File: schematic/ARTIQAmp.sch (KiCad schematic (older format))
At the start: 9 parts, among them J1 Power conneciton, J2 HD68, J3 HD68

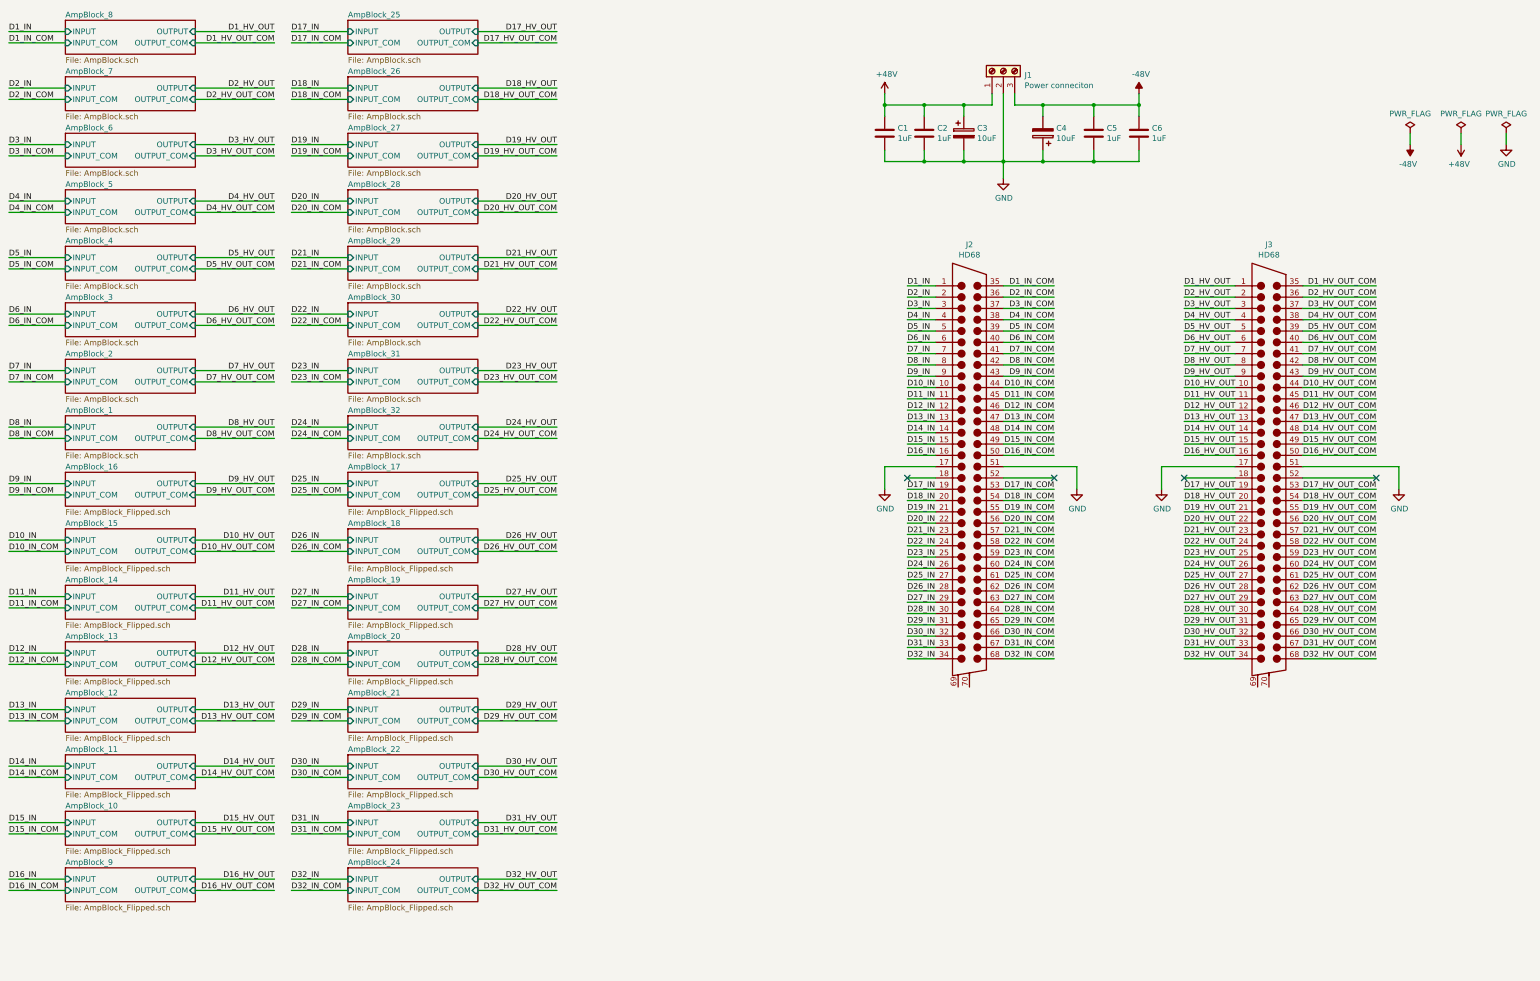
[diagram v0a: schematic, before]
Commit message: Board updates and starting to add more capacitors
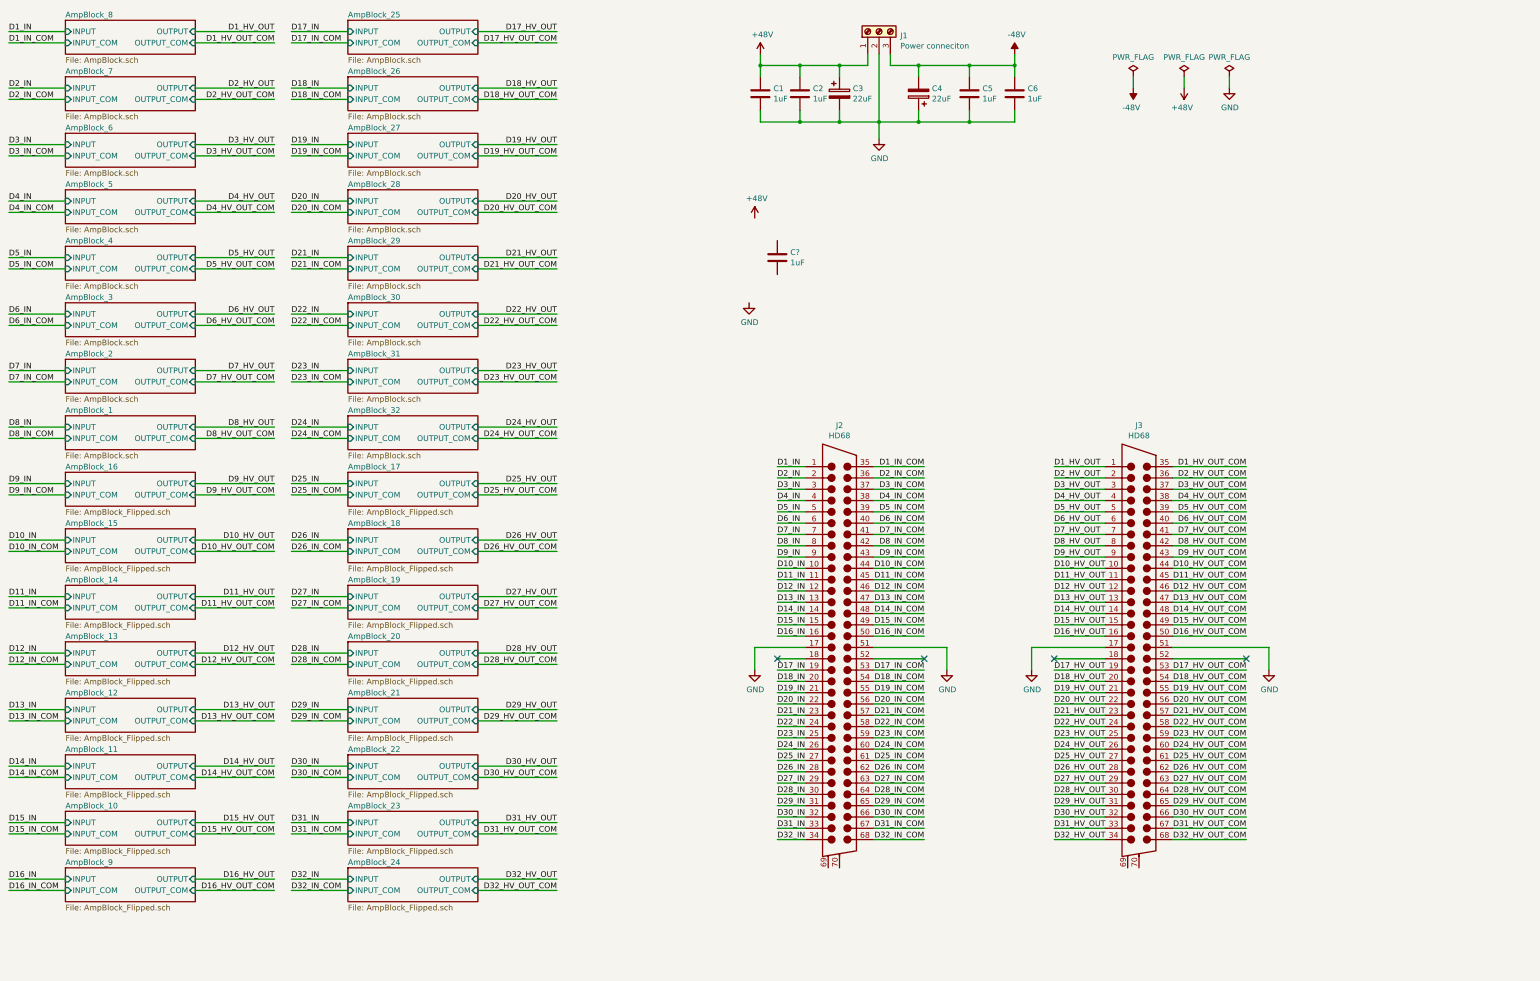
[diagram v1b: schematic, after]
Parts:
- added C?: 1uF, Capacitor_SMD:C_1206_3216Metric, symbol Device:C
- C1, C2, C5, C6: footprint Capacitor_SMD:C_0603_1608Metric -> Capacitor_SMD:C_1206_3216Metric
- C3, C4: value 10uF -> 22uF; footprint Capacitor_THT:CP_Radial_D6.3mm_P2.50mm -> Capacitor_THT:CP_Radial_D8.0mm_P3.50mm
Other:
- moved on the sheet: C1, C2, C3, C4, C5, C6, J1, J2, J3

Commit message: Many updates to layout; nearing final design
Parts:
- removed C?: 1uF, Capacitor_SMD:C_1206_3216Metric, symbol Device:C
- added C103, C104, C105, C106, C107, C108, C109, C110, C111, C112, C113, C114, C115, C116, C117, C118: 10uF, Capacitor_THT:CP_Radial_D6.3mm_P2.50mm, symbol Device:CP
- added R? (x2): 0R, Resistor_SMD:R_0603_1608Metric, symbol Device:R
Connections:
- net +48V: now also C103.1, C104.1, C105.1, C106.1, C107.1, C108.1, C109.1, C110.1
- net -48V: now also C111.2, C112.2, C113.2, C114.2, C115.2, C116.2, C117.2, C118.2
- net GND: now also C103.2, C104.2, C105.2, C106.2, C107.2, C108.2, C109.2, C110.2, C111.1, C112.1, C113.1, C114.1, C115.1, C116.1, C117.1, C118.1, R?.1, R?.1; no longer J2.17, J2.51, J3.17, J3.51
- new net: J2.17, J2.51, R?.2
- new net: J3.17, J3.51, R?.2

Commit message: Penultimate tweaks
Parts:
- gave numbers to parts that had none: 2
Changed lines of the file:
@@
 AR Path="/5CAE2E6A/5F95C626" Ref="R?"  Part="1"
 AR Path="/5CAE2EB0/5F95C626" Ref="R?"  Part="1"
-AR Path="/5F95C626" Ref="R?"  Part="1"
-F 0 "R?" V 8850 8700 50  0000 L CNN
+AR Path="/5F95C626" Ref="R257"  Part="1"
+F 0 "R257" V 8850 8700 50  0000 L CNN
 F 1 "0R" V 9050 8650 50  0000 L CNN
 F 2 "Resistor_SMD:R_0603_1608Metric" V 8880 8750 50  0001 C CNN
@@
 AR Path="/5CAE2E6A/5FA3F99C" Ref="R?"  Part="1"
 AR Path="/5CAE2EB0/5FA3F99C" Ref="R?"  Part="1"
-AR Path="/5FA3F99C" Ref="R?"  Part="1"
-F 0 "R?" V 11700 8700 50  0000 L CNN
+AR Path="/5FA3F99C" Ref="R258"  Part="1"
+F 0 "R258" V 11700 8700 50  0000 L CNN
 F 1 "0R" V 11900 8650 50  0000 L CNN
 F 2 "Resistor_SMD:R_0603_1608Metric" V 11730 8750 50  0001 C CNN

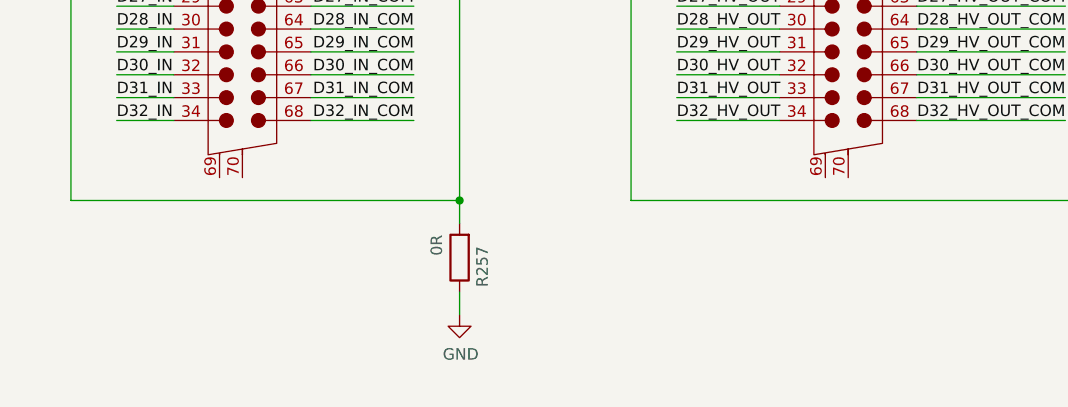
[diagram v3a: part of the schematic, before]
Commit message: Saftey commit before adding new shorting resistors
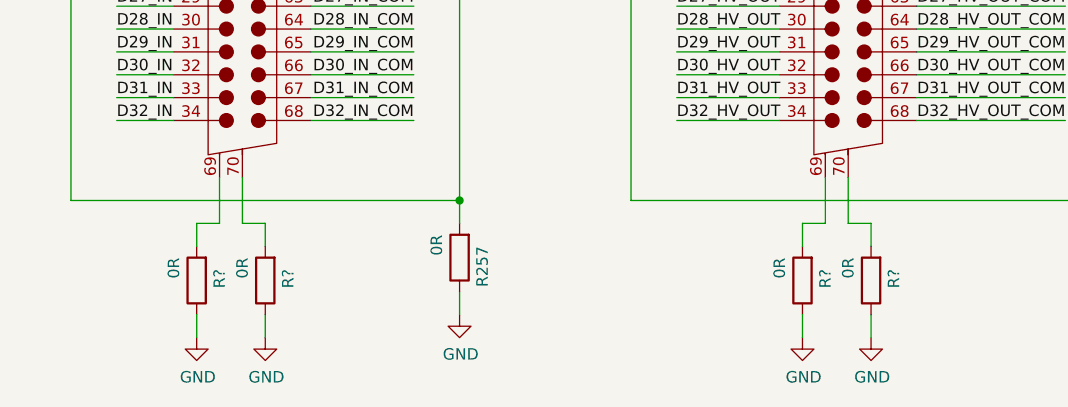
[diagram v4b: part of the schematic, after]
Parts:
- added R? (x4): 0R, Resistor_SMD:R_0805_2012Metric, symbol Device:R
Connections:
- net GND: now also R?.1, R?.1, R?.1, R?.1
- net at J2.69: now also R?.2
- net at J2.70: now also R?.2
- net at J3.69: now also R?.2
- net at J3.70: now also R?.2

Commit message: Design complete
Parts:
- gave numbers to parts that had none: 4
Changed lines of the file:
@@
 AR Path="/5CAE2E6A/5F9A57F6" Ref="R?"  Part="1"
 AR Path="/5CAE2EB0/5F9A57F6" Ref="R?"  Part="1"
-AR Path="/5F9A57F6" Ref="R?"  Part="1"
-F 0 "R?" V 7700 8800 50  0000 L CNN
+AR Path="/5F9A57F6" Ref="R259"  Part="1"
+F 0 "R259" V 7700 8800 50  0000 L CNN
 F 1 "0R" V 7900 8750 50  0000 L CNN
 F 2 "Resistor_SMD:R_0805_2012Metric" V 7730 8850 50  0001 C CNN
@@
 AR Path="/5CAE2E6A/5FA023DF" Ref="R?"  Part="1"
 AR Path="/5CAE2EB0/5FA023DF" Ref="R?"  Part="1"
-AR Path="/5FA023DF" Ref="R?"  Part="1"
-F 0 "R?" V 10350 8800 50  0000 L CNN
+AR Path="/5FA023DF" Ref="R261"  Part="1"
+F 0 "R261" V 10350 8800 50  0000 L CNN
 F 1 "0R" V 10550 8750 50  0000 L CNN
 F 2 "Resistor_SMD:R_0805_2012Metric" V 10380 8850 50  0001 C CNN
@@
 $EndComp
 $Comp
-L power:GND #PWR?
+L power:GND #PWR07
 U 1 1 5FA60732
 P 7800 9100
-F 0 "#PWR?" H 7800 8850 50  0001 C CNN
+F 0 "#PWR07" H 7800 8850 50  0001 C CNN
 F 1 "GND" H 7805 8927 50  0000 C CNN
 F 2 "" H 7800 9100 50  0001 C CNN
@@
 $EndComp
 $Comp
-L power:GND #PWR?
+L power:GND #PWR075
 U 1 1 5FA60AA2
 P 10450 9100
-F 0 "#PWR?" H 10450 8850 50  0001 C CNN
+F 0 "#PWR075" H 10450 8850 50  0001 C CNN
 F 1 "GND" H 10455 8927 50  0000 C CNN
 F 2 "" H 10450 9100 50  0001 C CNN
@@
 AR Path="/5CAE2E6A/5FBA78F5" Ref="R?"  Part="1"
 AR Path="/5CAE2EB0/5FBA78F5" Ref="R?"  Part="1"
-AR Path="/5FBA78F5" Ref="R?"  Part="1"
-F 0 "R?" V 8000 8800 50  0000 L CNN
+AR Path="/5FBA78F5" Ref="R260"  Part="1"
+F 0 "R260" V 8000 8800 50  0000 L CNN
 F 1 "0R" V 8200 8750 50  0000 L CNN
 F 2 "Resistor_SMD:R_0805_2012Metric" V 8030 8850 50  0001 C CNN
@@
 $EndComp
 $Comp
-L power:GND #PWR?
+L power:GND #PWR09
 U 1 1 5FBD619B
 P 8100 9100
-F 0 "#PWR?" H 8100 8850 50  0001 C CNN
+F 0 "#PWR09" H 8100 8850 50  0001 C CNN
 F 1 "GND" H 8105 8927 50  0000 C CNN
 F 2 "" H 8100 9100 50  0001 C CNN
@@
 AR Path="/5CAE2E6A/5FCBF84B" Ref="R?"  Part="1"
 AR Path="/5CAE2EB0/5FCBF84B" Ref="R?"  Part="1"
-AR Path="/5FCBF84B" Ref="R?"  Part="1"
-F 0 "R?" V 10650 8800 50  0000 L CNN
+AR Path="/5FCBF84B" Ref="R262"  Part="1"
+F 0 "R262" V 10650 8800 50  0000 L CNN
 F 1 "0R" V 10850 8750 50  0000 L CNN
 F 2 "Resistor_SMD:R_0805_2012Metric" V 10680 8850 50  0001 C CNN
@@
 	10750 8600 10750 8700
 $Comp
-L power:GND #PWR?
+L power:GND #PWR076
 U 1 1 5FD4F2D1
 P 10750 9100
-F 0 "#PWR?" H 10750 8850 50  0001 C CNN
+F 0 "#PWR076" H 10750 8850 50  0001 C CNN
 F 1 "GND" H 10755 8927 50  0000 C CNN
 F 2 "" H 10750 9100 50  0001 C CNN
